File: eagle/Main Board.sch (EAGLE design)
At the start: 2 parts

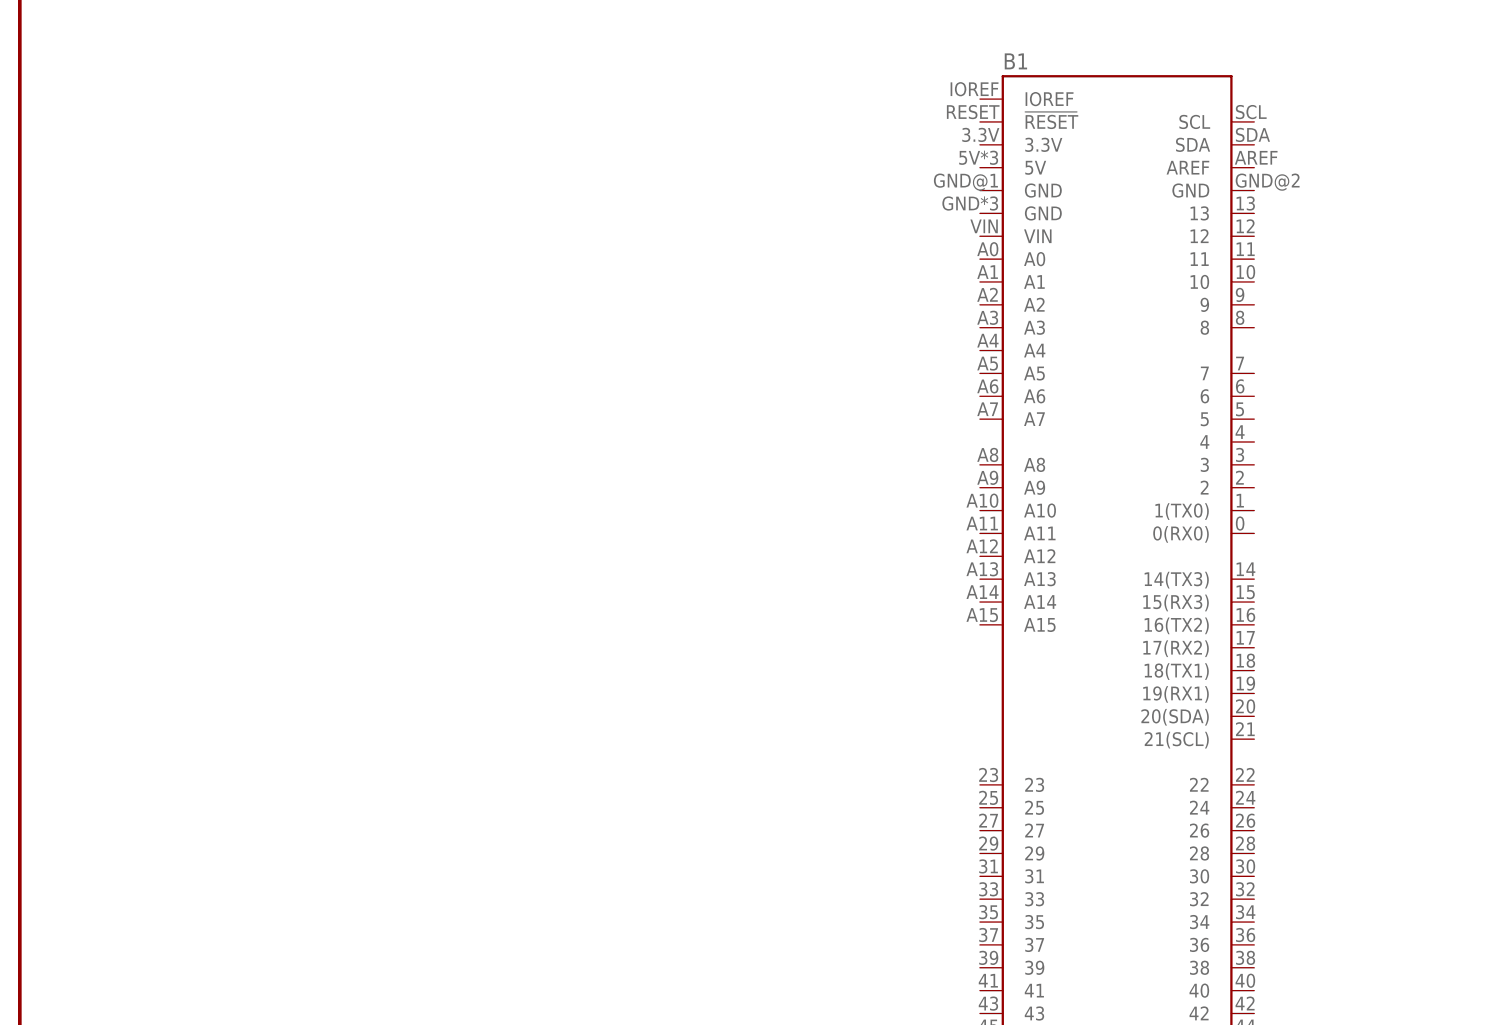
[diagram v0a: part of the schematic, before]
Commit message: Attached pins on MEGA to LED matrix port, created online of MEGA shield
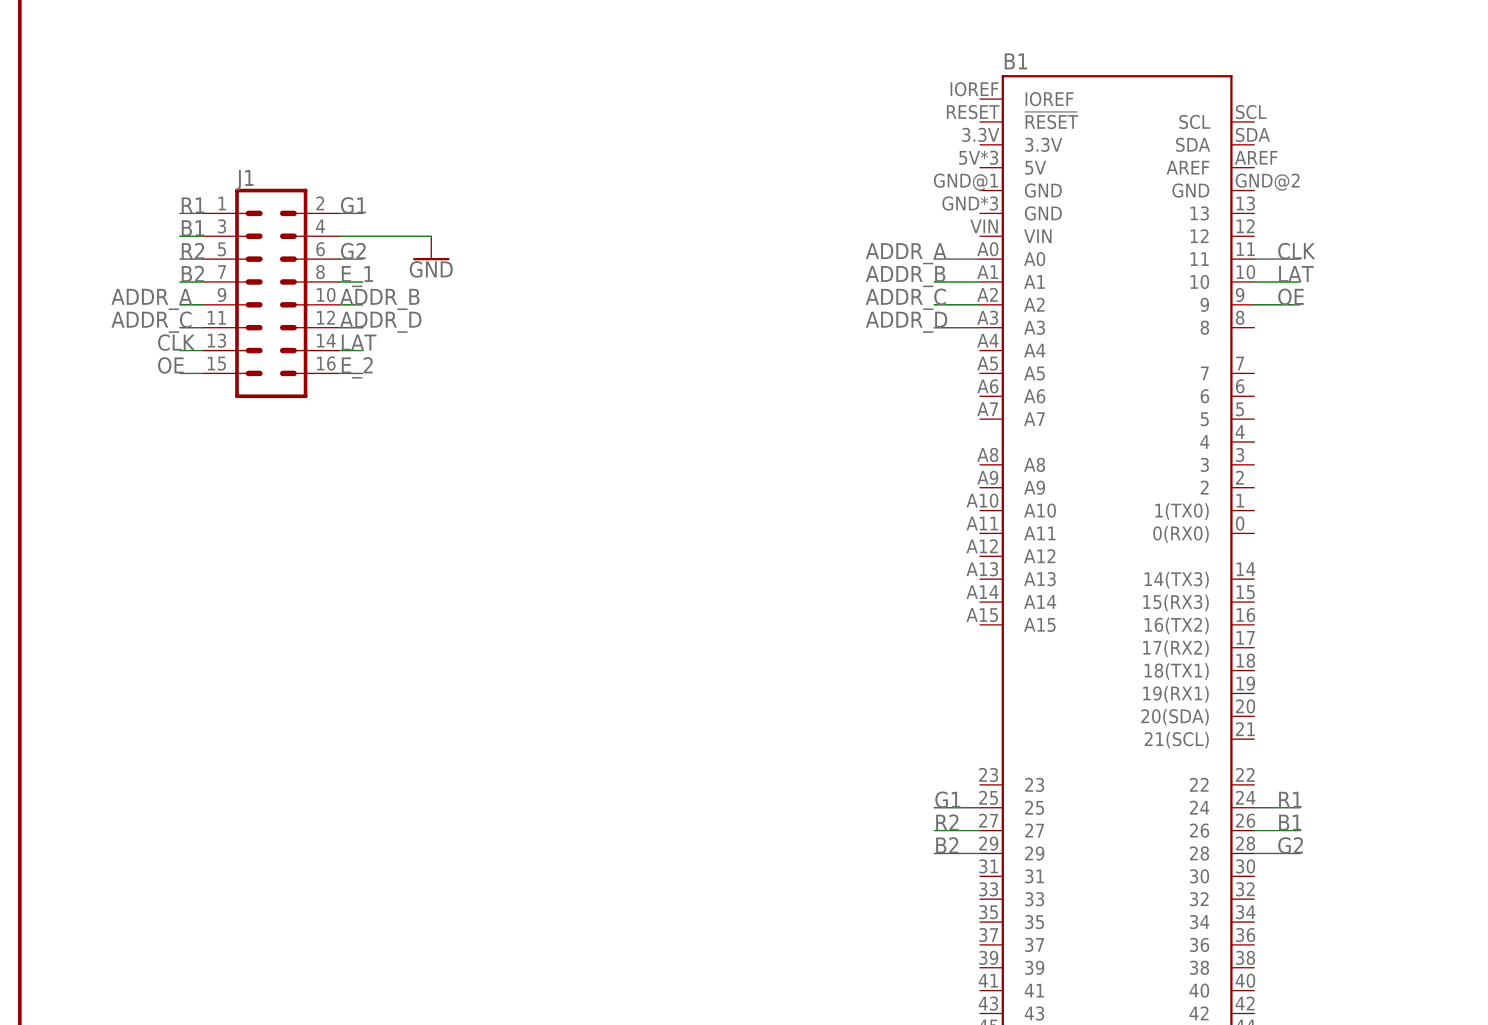
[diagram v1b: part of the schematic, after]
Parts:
- added J1: (no value), SparkFun-Connectors:CONN_08X2_SHROUD
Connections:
- new net ADDR_A: B1.A0, J1.9
- new net ADDR_B: B1.A1, J1.10
- new net ADDR_C: B1.A2, J1.11
- new net ADDR_D: B1.A3, J1.12
- new net B1: B1.26, J1.3
- new net B2: B1.29, J1.7
- new net CLK: B1.11, J1.13
- new net E_1: J1.8
- new net E_2: J1.16
- new net G1: B1.25, J1.2
- new net G2: B1.28, J1.6
- new net GND: J1.4
- new net LAT: B1.10, J1.14
- new net OE: B1.9, J1.15
- new net R1: B1.24, J1.1
- new net R2: B1.27, J1.5
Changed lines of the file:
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@@
 <part name="B1" library="SparkFun-Boards" deviceset="ARDUINO_MEGA_R3" device="FULL"/>
 <part name="FRAME1" library="SparkFun-Aesthetics" deviceset="FRAME-LETTER" device=""/>
+<part name="J1" library="SparkFun-Connectors" deviceset="CONN_08X2" device="_SHROUD"/>
+<part name="GND1" library="SparkFun-PowerSymbols" deviceset="GND" device=""/>
 </parts>
 <sheets>
@@
 <attribute name="REV" x="236.22" y="6.604" size="2.7432" layer="94" font="vector"/>
 </instance>
+<instance part="J1" gate="J1" x="27.94" y="144.78" smashed="yes">
+<attribute name="VALUE" x="24.13" y="132.334" size="1.778" layer="96" font="vector"/>
+<attribute name="NAME" x="24.13" y="157.988" size="1.778" layer="95" font="vector"/>
+</instance>
+<instance part="GND1" gate="1" x="45.72" y="149.86" smashed="yes">
+<attribute name="VALUE" x="45.72" y="149.606" size="1.778" layer="96" font="vector" align="top-center"/>
+</instance>
 </instances>
 <busses>
 </busses>
 <nets>
+<net name="R1" class="0">
+<segment>
+<pinref part="J1" gate="J1" pin="1"/>
+<wire x1="20.32" y1="154.94" x2="17.78" y2="154.94" width="0.1524" layer="91"/>
+<label x="17.78" y="154.94" size="1.778" layer="95"/>
+</segment>
+<segment>
+<pinref part="B1" gate="B1" pin="24"/>
+<wire x1="137.16" y1="88.9" x2="142.24" y2="88.9" width="0.1524" layer="91"/>
+<label x="139.7" y="88.9" size="1.778" layer="95"/>
+</segment>
+</net>
+<net name="G1" class="0">
+<segment>
+<pinref part="J1" gate="J1" pin="2"/>
+<wire x1="35.56" y1="154.94" x2="38.1" y2="154.94" width="0.1524" layer="91"/>
+<label x="35.56" y="154.94" size="1.778" layer="95"/>
+</segment>
+<segment>
+<pinref part="B1" gate="B1" pin="25"/>
+<wire x1="106.68" y1="88.9" x2="101.6" y2="88.9" width="0.1524" layer="91"/>
+<label x="101.6" y="88.9" size="1.778" layer="95"/>
+</segment>
+</net>
+<net name="B1" class="0">
+<segment>
+<pinref part="J1" gate="J1" pin="3"/>
+<wire x1="20.32" y1="152.4" x2="17.78" y2="152.4" width="0.1524" layer="91"/>
+<label x="17.78" y="152.4" size="1.778" layer="95"/>
+</segment>
+<segment>
+<pinref part="B1" gate="B1" pin="26"/>
+<wire x1="137.16" y1="86.36" x2="142.24" y2="86.36" width="0.1524" layer="91"/>
+<label x="139.7" y="86.36" size="1.778" layer="95"/>
+</segment>
+</net>
+<net name="R2" class="0">
+<segment>
+<pinref part="J1" gate="J1" pin="5"/>
+<wire x1="20.32" y1="149.86" x2="17.78" y2="149.86" width="0.1524" layer="91"/>
+<label x="17.78" y="149.86" size="1.778" layer="95"/>
+</segment>
+<segment>
+<pinref part="B1" gate="B1" pin="27"/>
+<wire x1="106.68" y1="86.36" x2="101.6" y2="86.36" width="0.1524" layer="91"/>
+<label x="101.6" y="86.36" size="1.778" layer="95"/>
+</segment>
+</net>
+<net name="G2" class="0">
+<segment>
+<pinref part="J1" gate="J1" pin="6"/>
+<wire x1="35.56" y1="149.86" x2="38.1" y2="149.86" width="0.1524" layer="91"/>
+<label x="35.56" y="149.86" size="1.778" layer="95"/>
+</segment>
+<segment>
+<pinref part="B1" gate="B1" pin="28"/>
+<wire x1="137.16" y1="83.82" x2="142.24" y2="83.82" width="0.1524" layer="91"/>
+<label x="139.7" y="83.82" size="1.778" layer="95"/>
+</segment>
+</net>
+<net name="E_1" class="0">
+<segment>
+<pinref part="J1" gate="J1" pin="8"/>
+<wire x1="35.56" y1="147.32" x2="38.1" y2="147.32" width="0.1524" layer="91"/>
+<label x="35.56" y="147.32" size="1.778" layer="95"/>
+</segment>
+</net>
+<net name="B2" class="0">
+<segment>
+<pinref part="J1" gate="J1" pin="7"/>
+<wire x1="20.32" y1="147.32" x2="17.78" y2="147.32" width="0.1524" layer="91"/>
+<label x="17.78" y="147.32" size="1.778" layer="95"/>
+</segment>
+<segment>
+<pinref part="B1" gate="B1" pin="29"/>
+<wire x1="106.68" y1="83.82" x2="101.6" y2="83.82" width="0.1524" layer="91"/>
+<label x="101.6" y="83.82" size="1.778" layer="95"/>
+</segment>
+</net>
+<net name="ADDR_A" class="0">
+<segment>
+<pinref part="J1" gate="J1" pin="9"/>
+<wire x1="20.32" y1="144.78" x2="17.78" y2="144.78" width="0.1524" layer="91"/>
+<label x="10.16" y="144.78" size="1.778" layer="95"/>
+</segment>
+<segment>
+<pinref part="B1" gate="B1" pin="A0"/>
+<wire x1="106.68" y1="149.86" x2="101.6" y2="149.86" width="0.1524" layer="91"/>
+<label x="93.98" y="149.86" size="1.778" layer="95"/>
+</segment>
+</net>
+<net name="ADDR_B" class="0">
+<segment>
+<pinref part="J1" gate="J1" pin="10"/>
+<wire x1="35.56" y1="144.78" x2="38.1" y2="144.78" width="0.1524" layer="91"/>
+<label x="35.56" y="144.78" size="1.778" layer="95"/>
+</segment>
+<segment>
+<pinref part="B1" gate="B1" pin="A1"/>
+<wire x1="106.68" y1="147.32" x2="101.6" y2="147.32" width="0.1524" layer="91"/>
+<label x="93.98" y="147.32" size="1.778" layer="95"/>
+</segment>
+</net>
+<net name="ADDR_D" class="0">
+<segment>
+<pinref part="J1" gate="J1" pin="12"/>
+<wire x1="35.56" y1="142.24" x2="38.1" y2="142.24" width="0.1524" layer="91"/>
+<label x="35.56" y="142.24" size="1.778" layer="95"/>
+</segment>
+<segment>
+<pinref part="B1" gate="B1" pin="A3"/>
+<wire x1="106.68" y1="142.24" x2="101.6" y2="142.24" width="0.1524" layer="91"/>
+<label x="93.98" y="142.24" size="1.778" layer="95"/>
+</segment>
+</net>
+<net name="ADDR_C" class="0">
+<segment>
+<pinref part="J1" gate="J1" pin="11"/>
+<wire x1="20.32" y1="142.24" x2="17.78" y2="142.24" width="0.1524" layer="91"/>
+<label x="10.16" y="142.24" size="1.778" layer="95"/>
+</segment>
+<segment>
+<pinref part="B1" gate="B1" pin="A2"/>
+<wire x1="106.68" y1="144.78" x2="101.6" y2="144.78" width="0.1524" layer="91"/>
+<label x="93.98" y="144.78" size="1.778" layer="95"/>
+</segment>
+</net>
+<net name="CLK" class="0">
+<segment>
+<pinref part="J1" gate="J1" pin="13"/>
+<wire x1="20.32" y1="139.7" x2="17.78" y2="139.7" width="0.1524" layer="91"/>
+<label x="15.24" y="139.7" size="1.778" layer="95"/>
+</segment>
+<segment>
+<pinref part="B1" gate="B1" pin="11"/>
+<wire x1="137.16" y1="149.86" x2="142.24" y2="149.86" width="0.1524" layer="91"/>
+<label x="139.7" y="149.86" size="1.778" layer="95"/>
+</segment>
+</net>
+<net name="OE" class="0">
+<segment>
+<pinref part="J1" gate="J1" pin="15"/>
+<wire x1="20.32" y1="137.16" x2="17.78" y2="137.16" width="0.1524" layer="91"/>
+<label x="15.24" y="137.16" size="1.778" layer="95"/>
+</segment>
+<segment>
+<pinref part="B1" gate="B1" pin="9"/>
+<wire x1="137.16" y1="144.78" x2="142.24" y2="144.78" width="0.1524" layer="91"/>
+<label x="139.7" y="144.78" size="1.778" layer="95"/>
+</segment>
+</net>
+<net name="E_2" class="0">
+<segment>
+<pinref part="J1" gate="J1" pin="16"/>
+<wire x1="35.56" y1="137.16" x2="38.1" y2="137.16" width="0.1524" layer="91"/>
+<label x="35.56" y="137.16" size="1.778" layer="95"/>
+</segment>
+</net>
+<net name="LAT" class="0">
+<segment>
+<pinref part="J1" gate="J1" pin="14"/>
+<wire x1="35.56" y1="139.7" x2="38.1" y2="139.7" width="0.1524" layer="91"/>
+<label x="35.56" y="139.7" size="1.778" layer="95"/>
+</segment>
+<segment>
+<pinref part="B1" gate="B1" pin="10"/>
+<wire x1="137.16" y1="147.32" x2="142.24" y2="147.32" width="0.1524" layer="91"/>
+<label x="139.7" y="147.32" size="1.778" layer="95"/>
+</segment>
+</net>
+<net name="GND" class="0">
+<segment>
+<pinref part="J1" gate="J1" pin="4"/>
+<pinref part="GND1" gate="1" pin="GND"/>
+<wire x1="35.56" y1="152.4" x2="45.72" y2="152.4" width="0.1524" layer="91"/>
+</segment>
+</net>
 </nets>
 </sheet>
